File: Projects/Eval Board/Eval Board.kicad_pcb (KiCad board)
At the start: 4 copper layers, 46 x 27.3 mm, 37 parts, among them J1 LO, J2 Q OUT, J3 I Out, J4 Q OUT, J6 Conn_01x02, J7 Conn_01x04, J8 Conn_01x05, U1 LTC5584

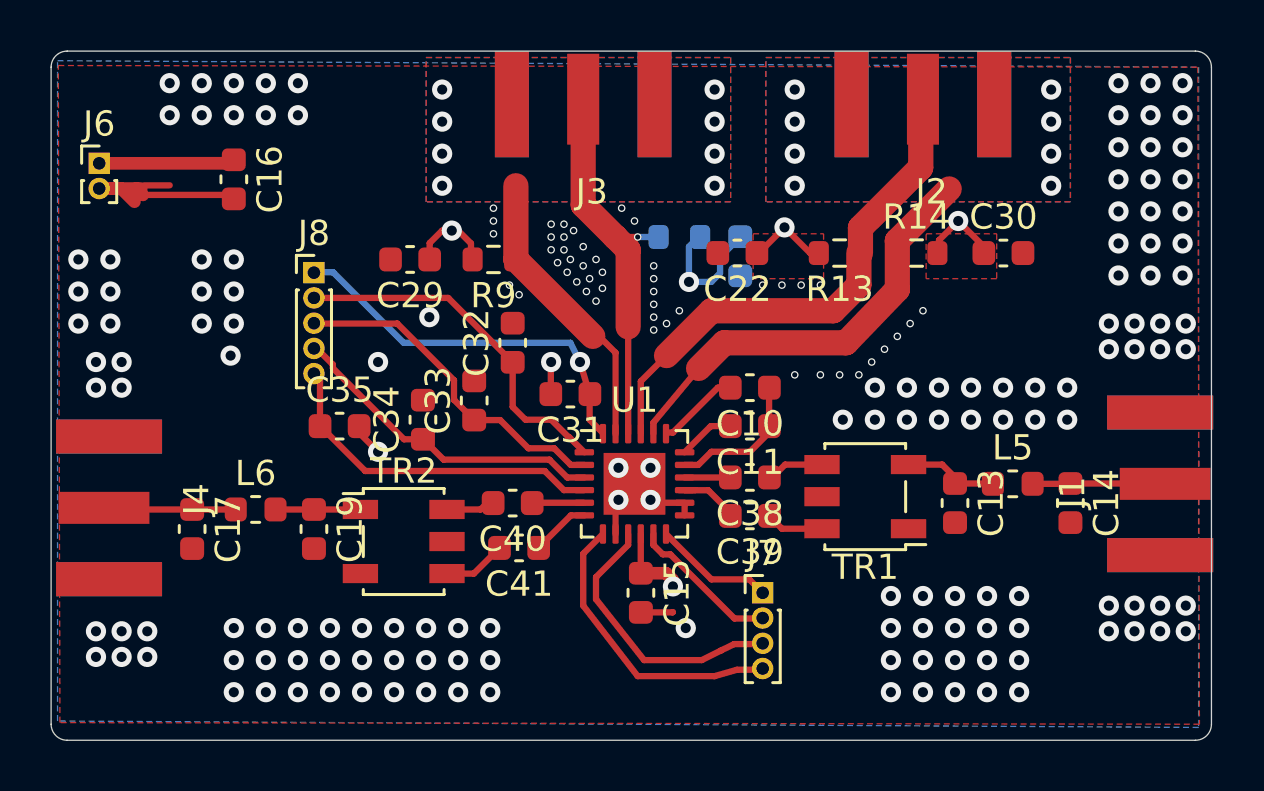
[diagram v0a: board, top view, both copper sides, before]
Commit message: fixed SMA connectors
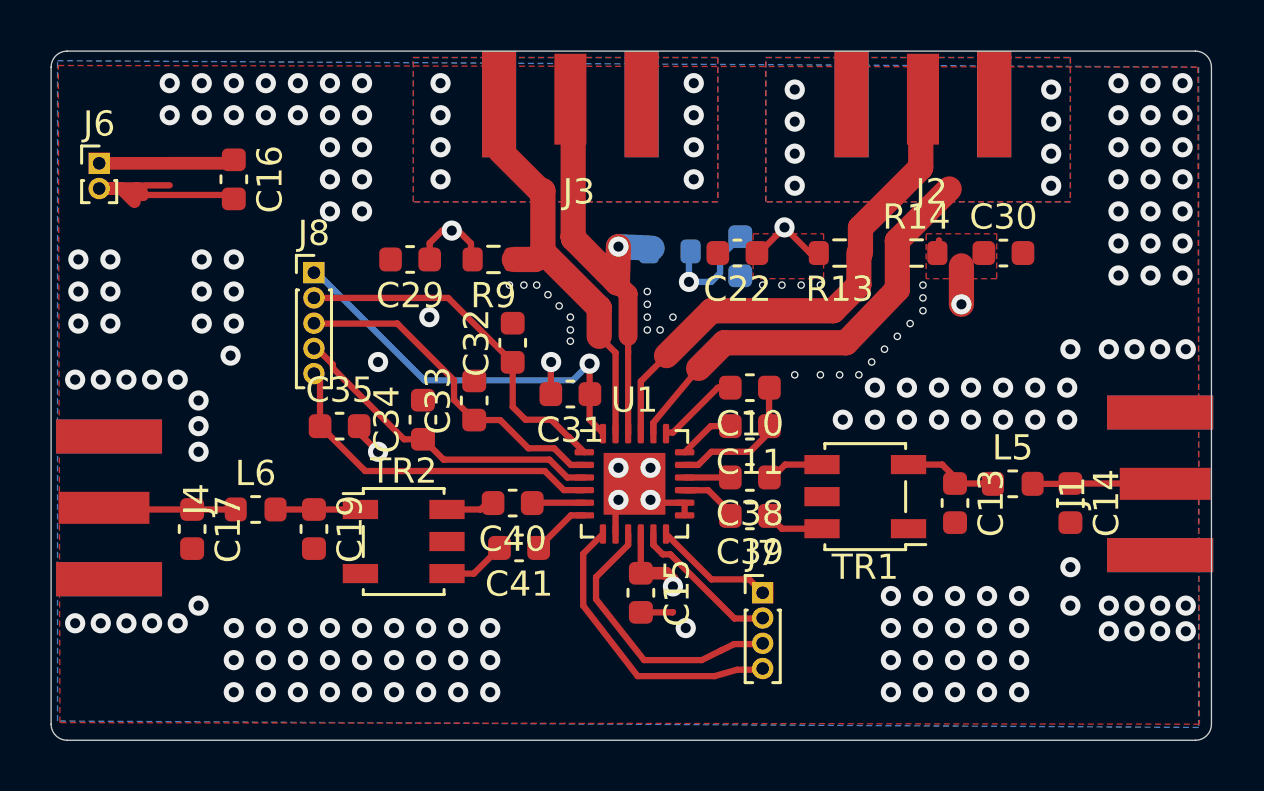
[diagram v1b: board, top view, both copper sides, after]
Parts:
- moved R11 0.69 mm to (197.0, 73.3)
- moved J3 0.51 mm to (193.0, 67.3)
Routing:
- net /I-: track 11.4 -> 14.4 mm
- net VCC: track 26.6 -> 25.1 mm
- net /I+: track 16.1 -> 17.1 mm
- net REF: track 15.2 -> 15.8 mm
- net GND: vias 188 -> 183
